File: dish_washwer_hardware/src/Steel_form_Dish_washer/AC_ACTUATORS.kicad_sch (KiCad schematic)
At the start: 61 parts, among them J10 DRAIN PUMP CONNECTOR, J11 WASH PUMP CONNECTOR, J12 BOILER HEATER CONNECTOR, J13 TANK HEATER, J14 peristaltic_pump_2, J15 peristaltic_pump_1, J9 SOLENOID CONNECTOR, K1 9-1440003-0, K2 9-1440003-0, K3 9-1440003-0, Q3 WST2N7002K, Q4 WST2N7002K, Q5 WST2N7002K, U10 MOC3021, U11 MOC3021, U12 MOC3021, U7 MOC3021, U8 MOC3021, U9 MOC3021

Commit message: complete schematic and assignment
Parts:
- removed F? (x2): Polyfuse, greencharge-footprints:BK250-600, symbol Device:Polyfuse
- removed J?: WATER PROBE SENSOR, greencharge-footprints:barrier_terminal_6PCV_04_006, symbol Connector:Conn_01x04_Male
- removed K?: 9-1440003-0, greencharge-footprints:TE_9-1440003-0, symbol 9-1440003-0:9-1440003-0
- removed RV? (x2): VDR-14D181K, Varistor:RV_Disc_D16.5mm_W6.7mm_P7.5mm, symbol Device:Varistor
- removed U?: HCPL3700M, Package_DIP:DIP-8_W7.62mm, symbol GCL_Integrated-Circuits:HCPL3700M
- removed U? (x2): 9-1393243-3, symbol GCL_Relays_Coils:9-1393243-3
- added F1, F2: Polyfuse, symbol Device:Polyfuse
- added J7: BOILER HEATER CONNECTOR, greencharge-footprints:barrier_terminal_6PCV_04_006, symbol Connector:Conn_01x04_Male
- added K4: 9-1440003-0, greencharge-footprints:TE_9-1440003-0, symbol 9-1440003-0:9-1440003-0
- added RV13, RV14: VDR-14D181K, Varistor:RV_Disc_D16.5mm_W6.7mm_P7.5mm, symbol Device:Varistor
- added U14, U5: 9-1393243-3, greencharge-footprints:9-1393243-3, symbol GCL_Relays_Coils:9-1393243-3
- added U6: HCPL3700M, Package_DIP:DIP-8_W7.62mm, symbol GCL_Integrated-Circuits:HCPL3700M
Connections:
- net +5V: now also U14.11 (COM), U6.8 (VCC)
- net E1: now also J7.1 (Pin_1), U14.A2, U5.A2
- net E2: now also J7.2 (Pin_2), U5.14 (NO)
- net E3: now also F1.2, J7.3 (Pin_3), RV13.1, U5.11 (COM)
- net GND: now also K4.2, U6.5 (GND)
- net L1: now also K1.3, K2.3, K3.3, F1.1, F2.1; no longer K1.4, K2.4, K3.4
- net NEUTRAL: now also RV13.2, RV14.2, U14.A1, U5.A1, U6.4 (AC)
- net WATER_LEVEL_PROBE: now also U6.6 (Vout)
- net Drain_Conn+ renamed DRAIN_CONN+
- net DRAIN_CONN+: now also K4.5
- new net: U5.12 (NC), U6.1 (AC)
- new net: K4.1, U14.14 (NO)
- new net DRAIN_SENSOR_PROBE: F2.2, J7.4 (Pin_4), RV14.1
- no-connect marks 11 -> 13
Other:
- note added: "The driver uses the reference probe E1 and the Drain_sensor prob to check if the max level of the water has been reached.If so the sensor turns on the relay and thus the drain pump"
- note added: "When the tank Level is low(below E@) the coil is de_energizeed. When the water level reaches E3 the coil is energized showing High Level.. E1 is used as a reference."
- note added: "When the tank is low, the NC contact is engaged. So the AC power flows through the optocoupler (HCPL3700M) and the output of the optocoupler is LOW. When the tank has water, the NO of the relay is engaged. No AC fkows via the optocoupler and the output is HIGH."
- note added: "to the MCU"
- note removed: "DARIN SENSOR PROBE"
- note removed: "DRAIN RELAY DRIVER"
- note removed: "LOGIC INPUT OUTPUT H L L H"
- note removed: "OPTOISOLATOR"
- note removed: "TO DRAIN PUMP DIRECT"
- note removed: "The driver uses the reference probe E1 and the Drain sensor probe to check if the max level of water has been reached. If so the sensors turn on the relay thus turning on the drain pump"
- note removed: "Vout will be read by MCU and it decides whether to turn on the pump or turn it off once its full"
- note removed: "When the tank is low(below E2) the coil is de_energized when water level reaches E3 the coil is energized showing a high level. E1 is used as a reference."
- note removed: "to allow complete draining of the tank during decomissioning."
- note removed: "when the tank level is low, the NC contact is engaged, so the AC power flows through the optocoupler (HCPL3700M) and the output of the optocoupler is low. When the tank has water, the NO of the relay is engaged. The AC power to the optocoupler is turned off and thus the optocoupler gives a HIGH output."
- moved on the sheet: D2, D5, D6, J10, J11, J13, J14, J15, J9, K1, K2, K3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

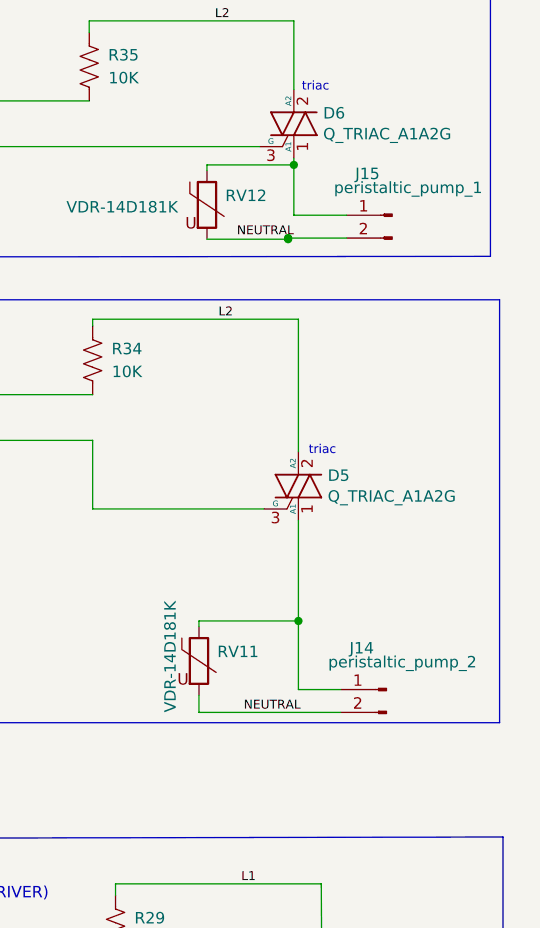
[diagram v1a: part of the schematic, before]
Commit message: updated layout high voltage
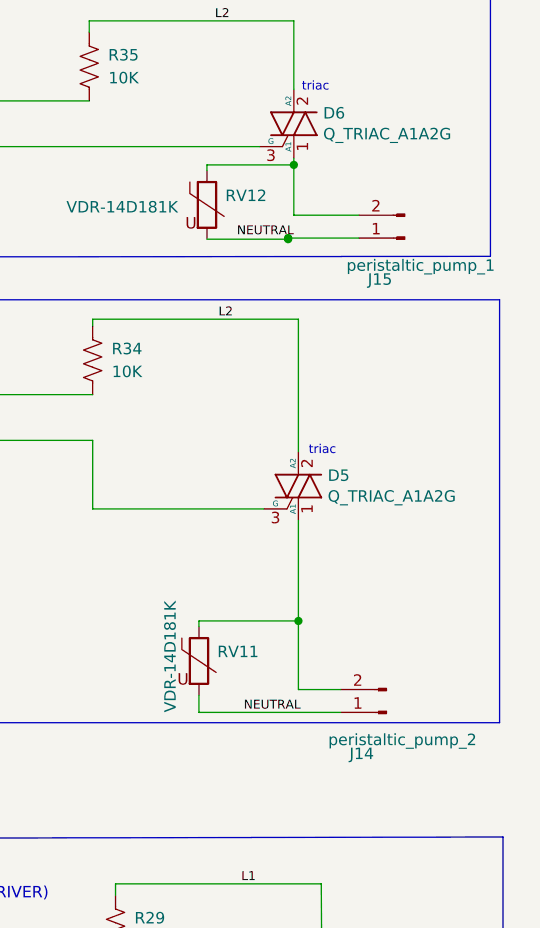
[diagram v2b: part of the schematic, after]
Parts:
- F1, F2: footprint (none) -> greencharge-footprints:BK250-600
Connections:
- net NEUTRAL: now also J14.1 (Pin_1), J15.1 (Pin_1); no longer J14.2 (Pin_2), J15.2 (Pin_2)
- net at D5.1 (A1), RV11.1: now also J14.2 (Pin_2); no longer J14.1 (Pin_1)
- net at D6.1 (A1), RV12.1: now also J15.2 (Pin_2); no longer J15.1 (Pin_1)
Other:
- moved on the sheet: J14, J15
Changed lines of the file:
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@@
+    (stroke (width 0) (type default) (color 0 0 0 0))
+  )
+  (wire (pts (xy 377.825 54.102) (xy 385.064 54.102))
     (stroke (width 0) (type default) (color 0 0 0 0))
   )
@@
     (stroke (width 0) (type default) (color 0 0 0 0))
   )
-  (wire (pts (xy 377.19 56.642) (xy 383.667 56.642))
+  (wire (pts (xy 377.19 56.642) (xy 385.064 56.642))
     (stroke (width 0) (type default) (color 0 0 0 0))
   )
@@
   )
   (wire (pts (xy 237.744 59.944) (xy 246.126 59.944))
-    (stroke (width 0) (type default) (color 0 0 0 0))
-  )
-  (wire (pts (xy 383.667 54.102) (xy 377.825 54.102))
     (stroke (width 0) (type default) (color 0 0 0 0))
   )
@@
     (pin "6")
   )
-  (symbol (lib_id "Connector:Conn_01x02_Male") (at 388.747 54.102 0) (mirror y) (unit 1)
-    (in_bom yes) (on_board yes)
-    (property "Reference" "J15" (id 0) (at 386.0038 49.5046 0))
-    (property "Value" "peristaltic_pump_1" (id 1) (at 390.525 51.054 0))
-    (property "Footprint" "greencharge-footprints:SHDR2W100P0X508_1X2_1070X900X1380P" (id 2) (at 388.747 54.102 0)
-      (effects (font (size 1.27 1.27)) hide)
-    )
-    (property "Datasheet" "~" (id 3) (at 388.747 54.102 0)
-      (effects (font (size 1.27 1.27)) hide)
-    )
-    (pin "1")
-    (pin "2")
-  )
-  (symbol (lib_id "Connector:Conn_01x02_Male") (at 388.112 106.807 0) (mirror y) (unit 1)
-    (in_bom yes) (on_board yes)
-    (property "Reference" "J14" (id 0) (at 385.3688 102.2096 0))
-    (property "Value" "peristaltic_pump_2" (id 1) (at 389.89 103.759 0))
-    (property "Footprint" "greencharge-footprints:SHDR2W100P0X508_1X2_1070X900X1380P" (id 2) (at 388.112 106.807 0)
-      (effects (font (size 1.27 1.27)) hide)
-    )
-    (property "Datasheet" "~" (id 3) (at 388.112 106.807 0)
+  (symbol (lib_id "Connector:Conn_01x02_Male") (at 390.144 56.642 180) (unit 1)
+    (in_bom yes) (on_board yes)
+    (property "Reference" "J15" (id 0) (at 387.4008 61.2394 0))
+    (property "Value" "peristaltic_pump_1" (id 1) (at 391.922 59.69 0))
+    (property "Footprint" "greencharge-footprints:SHDR2W100P0X508_1X2_1070X900X1380P" (id 2) (at 390.144 56.642 0)
+      (effects (font (size 1.27 1.27)) hide)
+    )
+    (property "Datasheet" "~" (id 3) (at 390.144 56.642 0)
+      (effects (font (size 1.27 1.27)) hide)
+    )
+    (pin "1")
+    (pin "2")
+  )
+  (symbol (lib_id "Connector:Conn_01x02_Male") (at 388.112 109.347 180) (unit 1)
+    (in_bom yes) (on_board yes)
+    (property "Reference" "J14" (id 0) (at 385.3688 113.9444 0))
+    (property "Value" "peristaltic_pump_2" (id 1) (at 389.89 112.395 0))
+    (property "Footprint" "greencharge-footprints:SHDR2W100P0X508_1X2_1070X900X1380P" (id 2) (at 388.112 109.347 0)
+      (effects (font (size 1.27 1.27)) hide)
+    )
+    (property "Datasheet" "~" (id 3) (at 388.112 109.347 0)
       (effects (font (size 1.27 1.27)) hide)
     )
@@
     (property "Reference" "F2" (id 0) (at 228.6 185.42 90))
     (property "Value" "Polyfuse" (id 1) (at 228.6 187.96 90))
-    (property "Footprint" "" (id 2) (at 233.68 190.5 0)
+    (property "Footprint" "greencharge-footprints:BK250-600" (id 2) (at 233.68 190.5 0)
       (effects (font (size 1.27 1.27)) (justify left) hide)
     )
@@
     (property "Reference" "F1" (id 0) (at 33.02 189.23 90))
     (property "Value" "Polyfuse" (id 1) (at 33.02 191.77 90))
-    (property "Footprint" "" (id 2) (at 38.1 194.31 0)
+    (property "Footprint" "greencharge-footprints:BK250-600" (id 2) (at 38.1 194.31 0)
       (effects (font (size 1.27 1.27)) (justify left) hide)
     )

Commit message: updating layout
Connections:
- net L1: now also K4.3
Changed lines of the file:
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@@
     (stroke (width 0) (type default) (color 0 0 0 0))
   )
-  (wire (pts (xy 337.82 217.17) (xy 342.9 217.17))
+  (wire (pts (xy 335.28 217.17) (xy 342.9 217.17))
     (stroke (width 0) (type default) (color 0 0 0 0))
   )
@@
     (stroke (width 0) (type default) (color 0 0 0 0))
   )
-  (wire (pts (xy 335.28 217.17) (xy 337.566 217.17))
-    (stroke (width 0) (type default) (color 0 0 0 0))
-  )

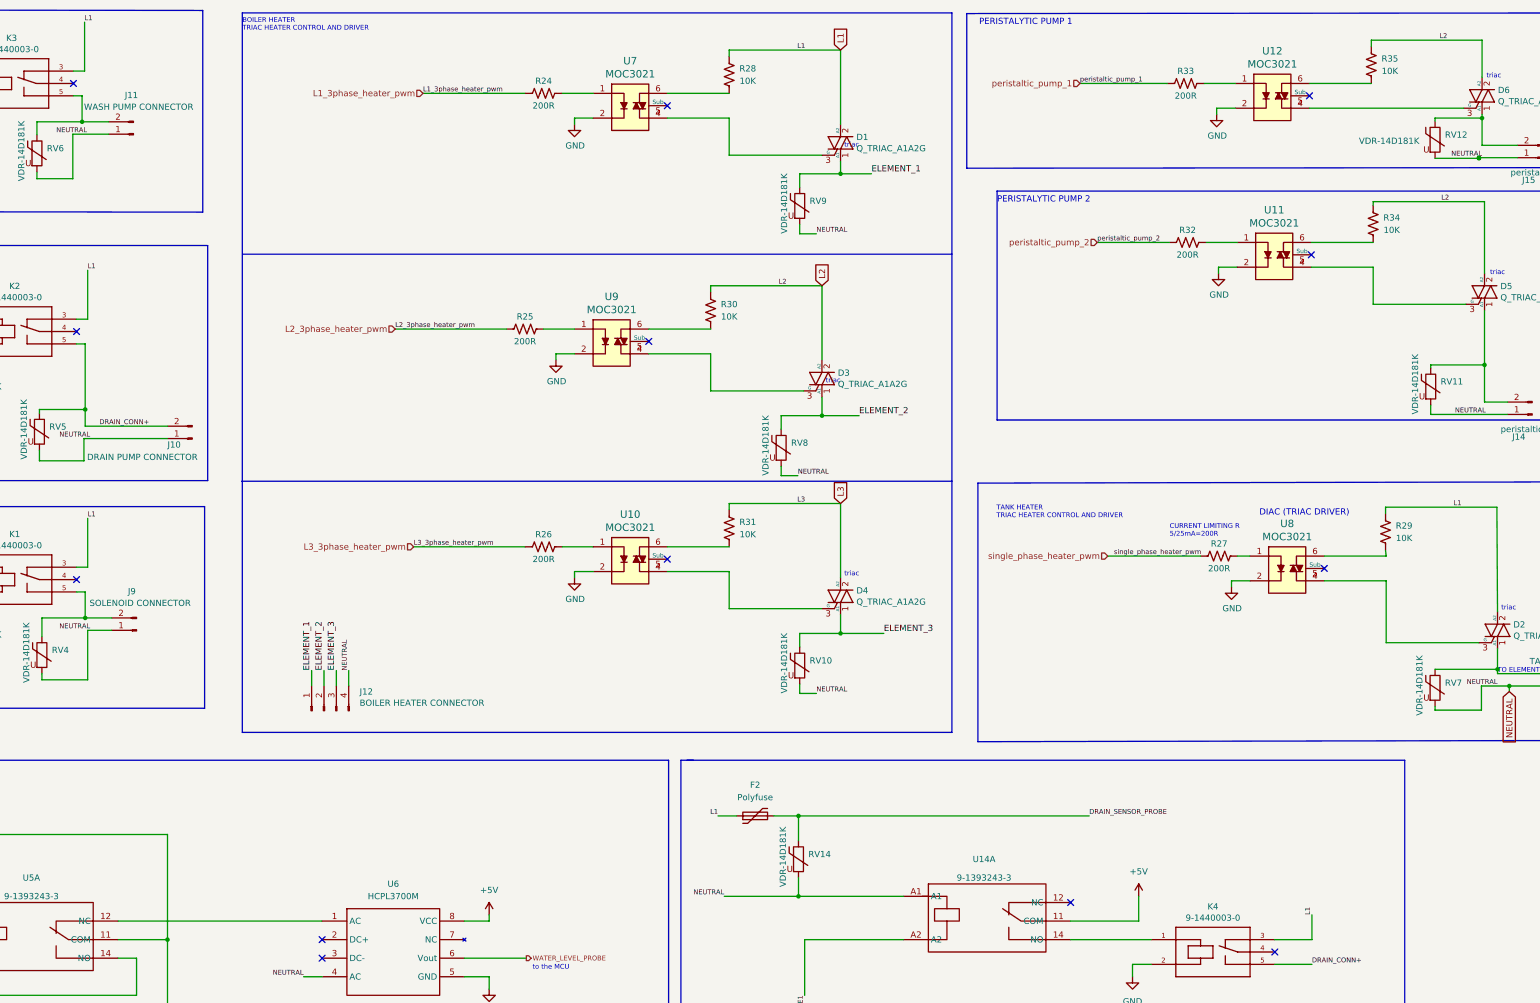
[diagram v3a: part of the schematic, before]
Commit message: updated layout
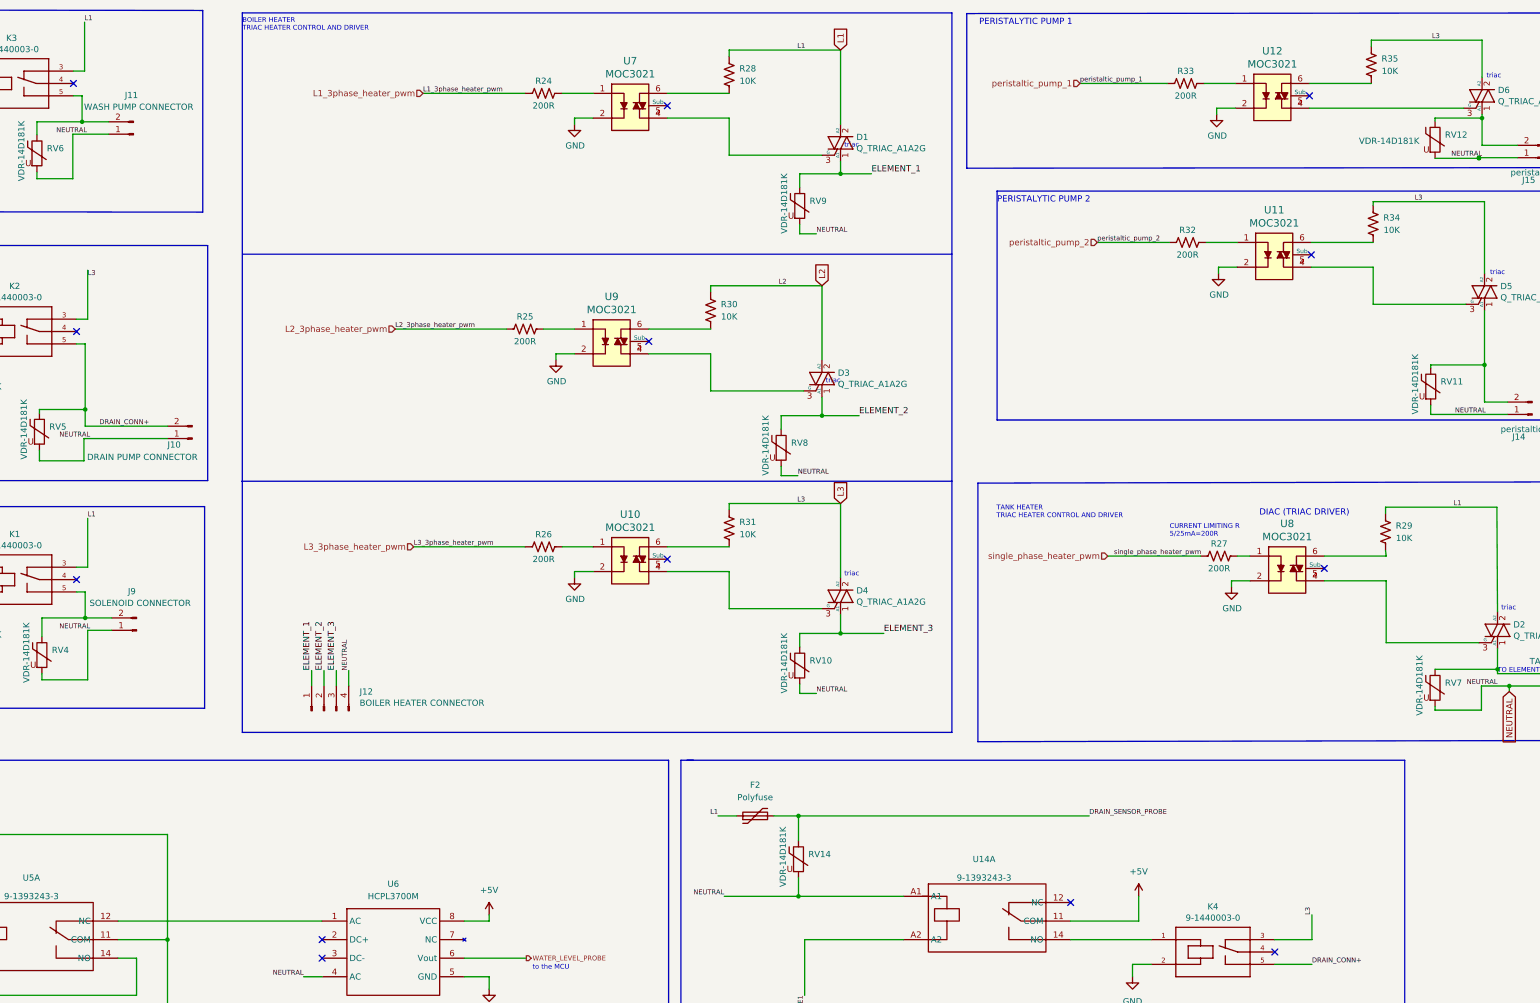
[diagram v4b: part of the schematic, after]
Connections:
- net L1: no longer K2.3, K4.3
- net L2: no longer D5.2 (A2), D6.2 (A2), R34.1, R35.1
- net L3: now also D5.2 (A2), D6.2 (A2), K2.3, K4.3, R34.1, R35.1
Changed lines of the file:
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@@
     (effects (font (size 0.9906 0.9906)) (justify right bottom))
+  )
+  (label "L3" (at 363.982 65.659 0)
+    (effects (font (size 0.9906 0.9906)) (justify left bottom))
   )
   (label "ELEMENT_3" (at 255.016 154.305 0)
@@
   (label "NEUTRAL" (at 381 165.1 180)
     (effects (font (size 0.9906 0.9906)) (justify right bottom))
-  )
-  (label "L1" (at 91.567 79.756 0)
-    (effects (font (size 0.9906 0.9906)) (justify left bottom))
   )
   (label "ELEMENT_2" (at 249.936 109.601 0)
@@
     (effects (font (size 0.9906 0.9906)) (justify left bottom))
   )
-  (label "L1" (at 342.9 212.09 90)
+  (label "L3" (at 342.9 212.09 90)
     (effects (font (size 0.9906 0.9906)) (justify left bottom))
   )
@@
     (effects (font (size 0.9906 0.9906)) (justify left bottom))
   )
-  (label "DRAIN_SENSOR_PROBE" (at 297.18 191.77 0)
+  (label "L3" (at 91.567 81.153 0)
     (effects (font (size 0.9906 0.9906)) (justify left bottom))
   )
-  (label "L2" (at 369.443 65.659 0)
+  (label "DRAIN_SENSOR_PROBE" (at 297.18 191.77 0)
     (effects (font (size 0.9906 0.9906)) (justify left bottom))
   )
@@
     (effects (font (size 0.9906 0.9906)) (justify right bottom))
   )
-  (label "L2" (at 369.062 32.512 0)
-    (effects (font (size 0.9906 0.9906)) (justify left bottom))
-  )
   (label "E1" (at 48.26 234.95 90)
     (effects (font (size 0.9906 0.9906)) (justify left bottom))
   )
+  (label "L3" (at 367.538 32.512 0)
+    (effects (font (size 0.9906 0.9906)) (justify left bottom))
+  )
